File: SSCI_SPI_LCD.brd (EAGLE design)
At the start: 110 x 100 mm, 29 parts, among them IC3 74LVC541_RGY, X1 TSW-108-02-S-S, X2 TSW-108-02-S-S

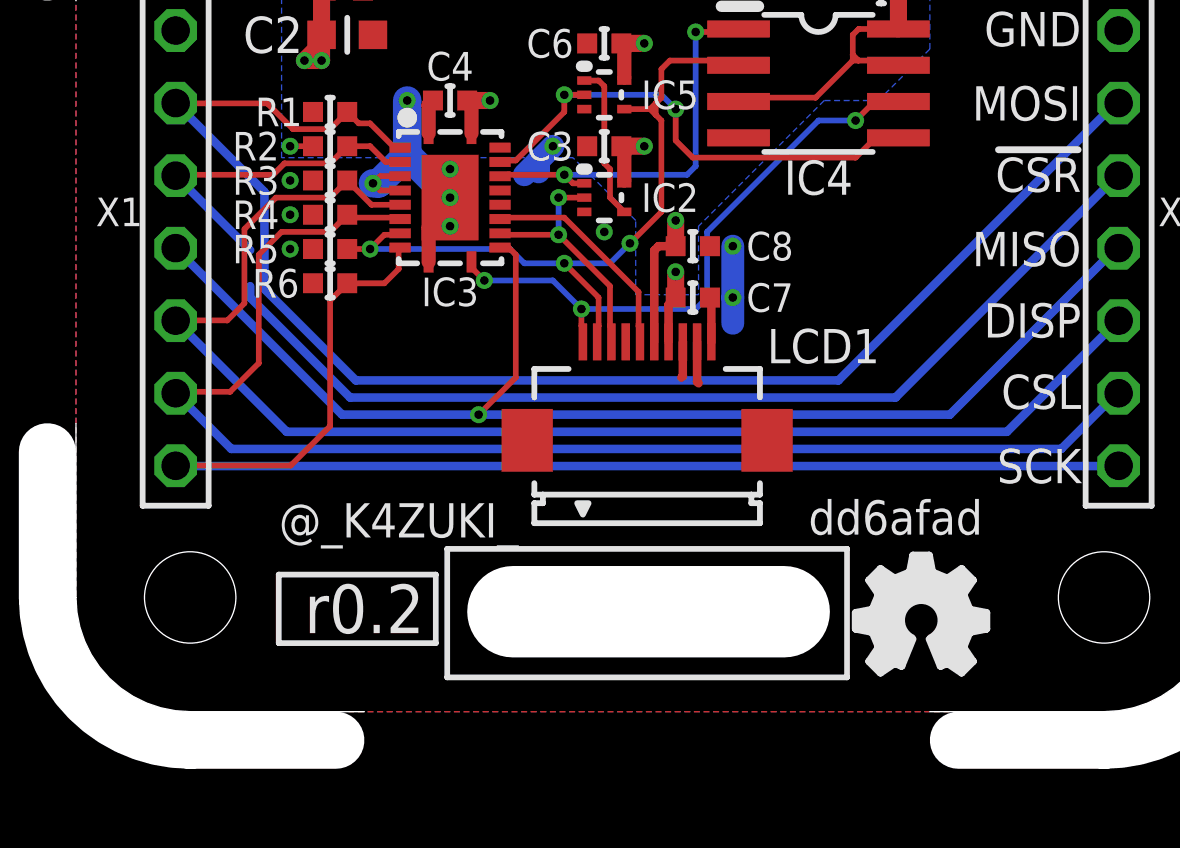
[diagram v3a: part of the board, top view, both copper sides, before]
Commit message: apply changes to panelising file
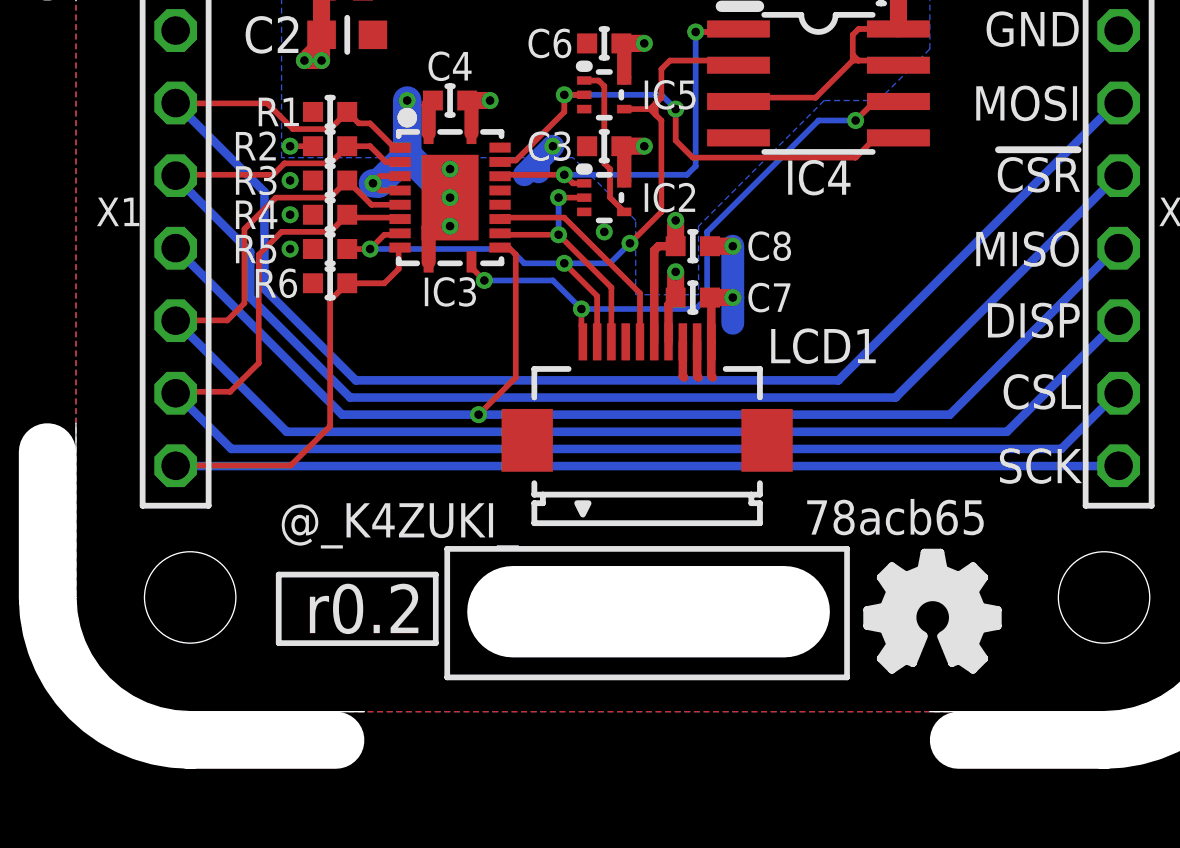
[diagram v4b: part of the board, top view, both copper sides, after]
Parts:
- GIT1: value dd6afad -> 78acb65
- moved ICON2 0.41 mm to (40.0, 13.3)
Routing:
- net GND: track 19.8 -> 22.4 mm
- net !CSR!: track 47.7 -> 48.9 mm
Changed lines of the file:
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@@
 <setting verticaltext="up"/>
 </settings>
-<grid distance="0.1" unitdist="mm" unit="mm" style="dots" multiple="1" display="yes" altdistance="0.1" altunitdist="mm" altunit="mm"/>
+<grid distance="0.1" unitdist="mm" unit="mm" style="dots" multiple="1" display="yes" altdistance="0.05" altunitdist="mm" altunit="mm"/>
 <layers>
 <layer number="1" name="Top" color="12" fill="0" visible="yes" active="yes"/>
@@
 <layer number="45" name="Holes" color="7" fill="1" visible="yes" active="yes"/>
 <layer number="46" name="Milling" color="3" fill="0" visible="yes" active="yes"/>
-<layer number="47" name="Measures" color="7" fill="1" visible="yes" active="yes"/>
+<layer number="47" name="Measures" color="7" fill="1" visible="no" active="yes"/>
 <layer number="48" name="Document" color="7" fill="1" visible="no" active="yes"/>
 <layer number="49" name="Reference" color="7" fill="1" visible="no" active="yes"/>
@@
 <layer number="100" name="Muster" color="7" fill="1" visible="no" active="no"/>
 <layer number="101" name="Attributes" color="7" fill="1" visible="no" active="yes"/>
-<layer number="102" name="Vscore" color="7" fill="1" visible="yes" active="yes"/>
+<layer number="102" name="Vscore" color="7" fill="1" visible="no" active="yes"/>
 <layer number="103" name="tMap" color="7" fill="1" visible="no" active="yes"/>
 <layer number="104" name="Name" color="7" fill="1" visible="no" active="yes"/>
@@
 <wire x1="30.5" y1="25.5" x2="30.5" y2="23.8" width="0" layer="41"/>
 <wire x1="19.8" y1="28.5" x2="20.3" y2="28.5" width="0" layer="41"/>
-<wire x1="21.4" y1="30" x2="21.4" y2="30.5" width="0" layer="41"/>
-<wire x1="20.7" y1="30" x2="20.7" y2="30.5" width="0" layer="41"/>
-<wire x1="20.7" y1="25.5" x2="20.7" y2="26" width="0" layer="41"/>
-<wire x1="21.4" y1="25.5" x2="21.4" y2="26" width="0" layer="41"/>
+<wire x1="22.8" y1="30" x2="22.8" y2="30.5" width="0" layer="41"/>
+<wire x1="21.9" y1="30" x2="21.9" y2="30.5" width="0" layer="41"/>
+<wire x1="21.9" y1="25.5" x2="21.9" y2="26" width="0" layer="41"/>
+<wire x1="22.8" y1="25.6" x2="22.8" y2="26.1" width="0" layer="41"/>
 <wire x1="21.3" y1="25.2" x2="20.8" y2="25.2" width="0" layer="41"/>
-<wire x1="20.8" y1="29.5" x2="22.8" y2="29.5" width="0" layer="41"/>
-<wire x1="22.8" y1="29.5" x2="22.8" y2="26.5" width="0" layer="41"/>
-<wire x1="20.8" y1="26.5" x2="20.8" y2="29.5" width="0" layer="41"/>
+<wire x1="22.1" y1="29.5" x2="24.1" y2="29.5" width="0" layer="41"/>
+<wire x1="24.1" y1="29.5" x2="24.1" y2="26.5" width="0" layer="41"/>
+<wire x1="22.1" y1="26.5" x2="22.1" y2="29.5" width="0" layer="41"/>
 <wire x1="32.6" y1="23.6" x2="32.6" y2="22.3" width="0" layer="41"/>
 <dimension x1="0" y1="0" x2="0" y2="10" x3="-8.6" y3="5" textsize="1.778" layer="47"/>
@@
 <text x="45.2" y="18.6" size="1.2" layer="21" ratio="20" align="center-right">SCK</text>
 <dimension x1="13.49" y1="27.5" x2="46.51" y2="27.5" x3="30" y3="2.9" textsize="1.2" textratio="20" layer="47" dtype="horizontal" unit="inch" visible="yes"/>
+<wire x1="31.9" y1="24.1" x2="32.5" y2="24.1" width="0" layer="41"/>
 </plain>
 <attributes>
@@
 <attribute name="NOT_COMPONENT" value="YES" x="14" y="14" size="1.778" layer="27" rot="R270" display="off"/>
 </element>
-<element name="GIT1" library="git-revision" package="GIT-REVISION_1.2" value="dd6afad" x="38.7" y="16.8">
+<element name="GIT1" library="git-revision" package="GIT-REVISION_1.2" value="78acb65" x="38.7" y="16.8">
 <attribute name="NOT_COMPONENT" value="YES" x="38.7" y="16.8" size="1.778" layer="27" display="off"/>
 </element>
@@
 <attribute name="VALUE" x="31.6" y="26.3" size="1" layer="27" font="vector" align="center"/>
 </element>
-<element name="ICON2" library="mylib" package="ICON_OSHW" value="" x="39.6" y="13.2">
-<attribute name="NOT_COMPONENT" value="YES" x="39.6" y="13.2" size="2" layer="27" ratio="20" display="off"/>
+<element name="ICON2" library="mylib" package="ICON_OSHW" value="" x="40" y="13.3">
+<attribute name="NOT_COMPONENT" value="YES" x="40" y="13.3" size="2" layer="27" ratio="20" display="off"/>
 </element>
 </elements>
@@
 <via x="17.5" y="27.4" extent="1-16" drill="0.3"/>
 <wire x1="31.25" y1="22.95" x2="31.25" y2="21.75" width="0.3" layer="1"/>
-<wire x1="31.25" y1="21.75" x2="31.2" y2="21.7" width="0.3" layer="1"/>
-<wire x1="31.75" y1="22.95" x2="31.75" y2="21.55" width="0.3" layer="1"/>
-<wire x1="31.75" y1="21.55" x2="31.8" y2="21.5" width="0.3" layer="1"/>
+<wire x1="31.25" y1="21.75" x2="31.3" y2="21.7" width="0.3" layer="1"/>
+<wire x1="31.75" y1="22.95" x2="31.75" y2="21.75" width="0.3" layer="1"/>
+<wire x1="31.75" y1="21.75" x2="31.8" y2="21.7" width="0.3" layer="1"/>
 <wire x1="32.25" y1="22.95" x2="32.25" y2="24.45" width="0.3" layer="1"/>
 <wire x1="32.25" y1="24.45" x2="32.2" y2="24.5" width="0.3" layer="1"/>
@@
 <wire x1="26.2" y1="29.3" x2="26.2" y2="28.9" width="0.8" layer="16"/>
 <wire x1="26.2" y1="29.3" x2="25.7" y2="28.8" width="0.8" layer="16"/>
+<wire x1="32.25" y1="22.95" x2="32.25" y2="21.75" width="0.3" layer="1"/>
+<wire x1="32.25" y1="21.75" x2="32.3" y2="21.7" width="0.3" layer="1"/>
+<wire x1="33" y1="24.5" x2="32.2" y2="24.5" width="0.6" layer="1"/>
+<wire x1="33" y1="26.3" x2="32.2" y2="26.3" width="0.6" layer="1"/>
 </signal>
 <signal name="5V">
@@
 <wire x1="13.52" y1="28.8" x2="13.49" y2="28.77" width="0.2" layer="1"/>
 <wire x1="19.6" y1="21" x2="16.1" y2="24.5" width="0.3" layer="16"/>
-<wire x1="16.1" y1="24.5" x2="16.1" y2="24.9" width="0.3" layer="16"/>
-<wire x1="16.1" y1="26.16" x2="13.49" y2="28.77" width="0.3" layer="16"/>
-<wire x1="16.1" y1="24.9" x2="16.1" y2="26.16" width="0" layer="19" extent="16-16"/>
+<wire x1="16.1" y1="24.5" x2="16.1" y2="26.1" width="0.3" layer="16"/>
+<wire x1="13.49" y1="28.77" x2="13.49" y2="28.71" width="0.3" layer="16"/>
+<wire x1="13.49" y1="28.71" x2="16.1" y2="26.1" width="0.3" layer="16"/>
 </signal>
 <signal name="MOSI">
@@
 <via x="20.3" y="26.2" extent="1-16" drill="0.3"/>
 <wire x1="25.2" y1="26.2" x2="25.7" y2="25.7" width="0.2" layer="16"/>
-<wire x1="28.25" y1="22.95" x2="28.25" y2="23.45" width="0.2" layer="1"/>
-<wire x1="28.25" y1="23.45" x2="28.3" y2="23.5" width="0.2" layer="1"/>
-<wire x1="28.3" y1="23.5" x2="28.3" y2="24.5" width="0.2" layer="1"/>
-<wire x1="28.3" y1="24.5" x2="27.1" y2="25.7" width="0.2" layer="1"/>
+<wire x1="28.25" y1="22.95" x2="28.25" y2="24.55" width="0.2" layer="1"/>
+<wire x1="28.25" y1="24.55" x2="27.1" y2="25.7" width="0.2" layer="1"/>
 <via x="27.1" y="25.7" extent="1-16" drill="0.3"/>
 <wire x1="33.2" y1="32.635" x2="32.365" y2="32.635" width="0.2" layer="1"/>
@@
 <contactref element="LCD1" pad="3"/>
 <contactref element="IC3" pad="13"/>
-<wire x1="28.75" y1="22.95" x2="28.75" y2="23.45" width="0.2" layer="1"/>
-<wire x1="28.75" y1="23.45" x2="28.7" y2="23.5" width="0.2" layer="1"/>
+<wire x1="28.75" y1="22.95" x2="28.75" y2="24.85" width="0.2" layer="1"/>
 <wire x1="24.85" y1="26.75" x2="24.9" y2="26.7" width="0.2" layer="1"/>
 <wire x1="24.9" y1="26.7" x2="26.9" y2="26.7" width="0.2" layer="1"/>
@@
 <via x="26.9" y="28" extent="1-16" drill="0.3"/>
 <via x="26.9" y="26.7" extent="1-16" drill="0.3"/>
-<wire x1="28.7" y1="23.5" x2="28.7" y2="24.9" width="0.2" layer="1"/>
-<wire x1="28.7" y1="24.9" x2="26.9" y2="26.7" width="0.2" layer="1"/>
+<wire x1="28.75" y1="24.85" x2="26.9" y2="26.7" width="0.2" layer="1"/>
 </signal>
 <signal name="DISP-">
@@
 <wire x1="24.85" y1="27.25" x2="24.9" y2="27.3" width="0.2" layer="1"/>
 <wire x1="24.9" y1="27.3" x2="27.1" y2="27.3" width="0.2" layer="1"/>
-<wire x1="29.75" y1="22.95" x2="29.75" y2="23.45" width="0.2" layer="1"/>
-<wire x1="29.75" y1="23.45" x2="29.7" y2="23.5" width="0.2" layer="1"/>
-<wire x1="29.7" y1="23.5" x2="29.7" y2="24.7" width="0.2" layer="1"/>
-<wire x1="29.7" y1="24.7" x2="27.1" y2="27.3" width="0.2" layer="1"/>
+<wire x1="29.75" y1="22.95" x2="29.75" y2="24.65" width="0.2" layer="1"/>
+<wire x1="29.75" y1="24.65" x2="27.1" y2="27.3" width="0.2" layer="1"/>
 </signal>
 </signals>

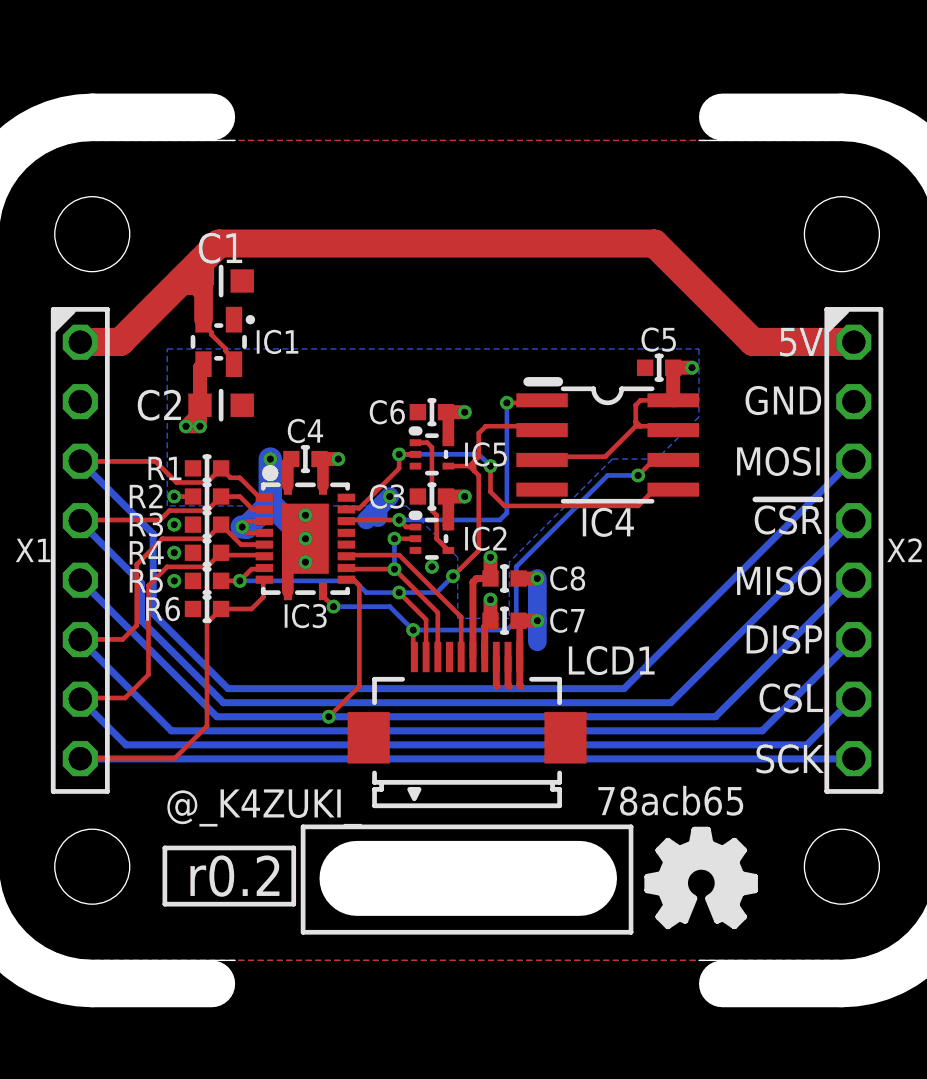
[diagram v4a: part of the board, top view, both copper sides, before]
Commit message: add MinLab icon; moves
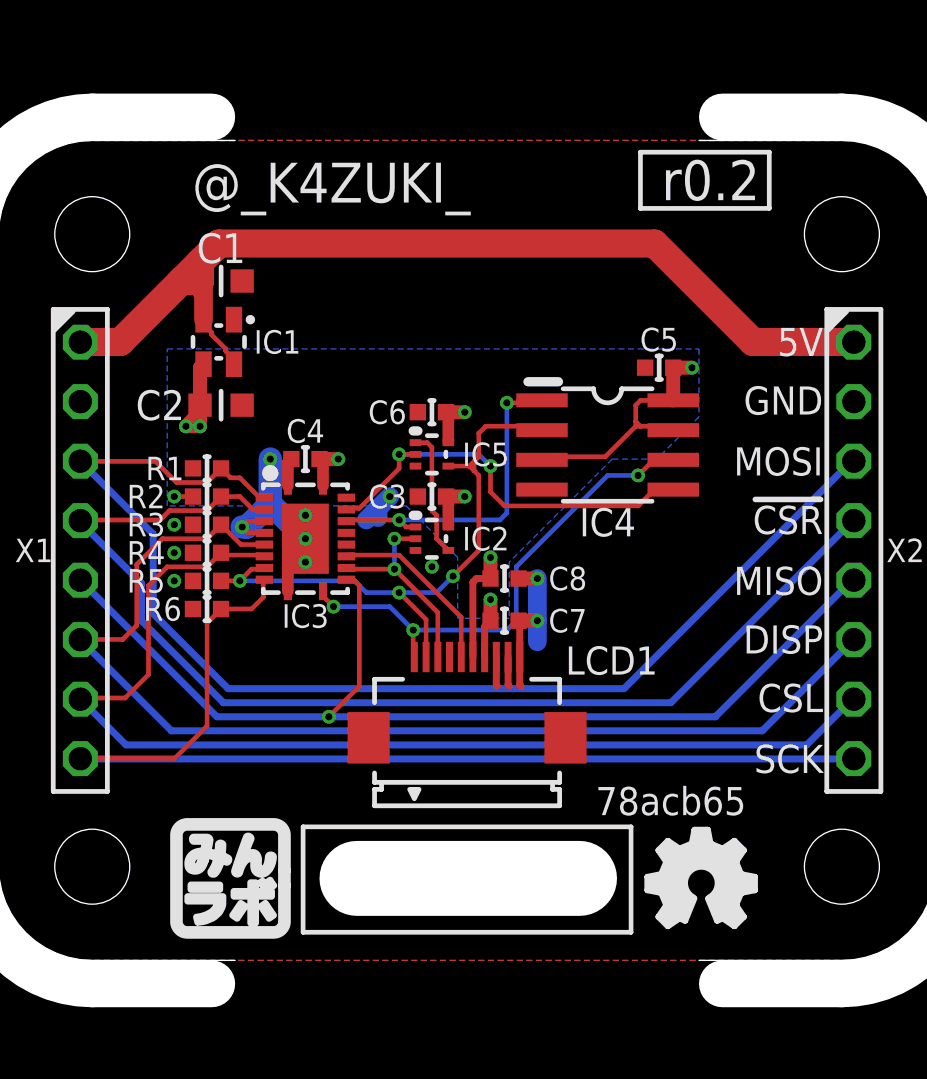
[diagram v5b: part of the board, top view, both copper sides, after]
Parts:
- added I1: (no value), mylib:ICON_MINLAB_5.2MM
- moved ICON1 36.0 mm to (40.5, 43.3)
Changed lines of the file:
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@@
 <dimension x1="0" y1="0" x2="110" y2="0" x3="55" y3="-12.4" textsize="2" textratio="20" layer="47" dtype="horizontal"/>
 <dimension x1="0" y1="0" x2="0" y2="100" x3="-12.6" y3="50" textsize="2" textratio="20" layer="47" dtype="vertical"/>
-<text x="21.3" y="16.7" size="1.2" layer="21" ratio="20" align="center">@_K4ZUKI_</text>
+<text x="24.2" y="43.2" size="1.7" layer="21" ratio="12" align="center">@_K4ZUKI_</text>
 <wire x1="10" y1="45" x2="50" y2="45" width="0.8" layer="41"/>
 <wire x1="10" y1="45" x2="50" y2="45" width="0.8" layer="42"/>
@@
 <attribute name="NOT_COMPONENT" value="YES" x="38.7" y="16.8" size="1.778" layer="27" display="off"/>
 </element>
-<element name="ICON1" library="mylib" package="ICON_REVISION1.7" value="r0.2" x="20.2" y="13.6">
-<attribute name="NOT_COMPONENT" value="YES" x="20.2" y="13.6" size="1.778" layer="27" display="off"/>
+<element name="ICON1" library="mylib" package="ICON_REVISION1.7" value="r0.2" x="40.5" y="43.3">
+<attribute name="NOT_COMPONENT" value="YES" x="40.5" y="43.3" size="1.778" layer="27" display="off"/>
 </element>
 <element name="X1" library="con-samtec.local" package="TSW-108-02-S-S" value="TSW-108-02-S-S" x="13.49" y="27.5" smashed="yes" rot="R90">
@@
 <attribute name="NOT_COMPONENT" value="YES" x="40" y="13.3" size="2" layer="27" ratio="20" display="off"/>
 </element>
+<element name="I1" library="mylib" package="ICON_MINLAB_5.2MM" value="" x="17.4" y="11">
+<attribute name="NOT_COMPONENT" value="YES" x="17.4" y="11" size="1.2" layer="27" ratio="20" display="off"/>
+</element>
 </elements>

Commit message: update libraries; update panelise; update gerbers
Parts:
- GIT1: value 78acb65 -> fd68d81
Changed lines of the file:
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@@
 <attribute name="NAME" x="34.2" y="22.2" size="1.2" layer="25" font="vector" ratio="17"/>
 <attribute name="VALUE" x="25.9" y="22.2" size="1.2" layer="27" font="vector" ratio="17" rot="R180"/>
+<attribute name="MOUSER" value="798-FH12-10S-0.5SH55" x="30" y="19.5" size="1.778" layer="27" display="off"/>
+<attribute name="DIGIKEY" value="HFJ110CT-ND" x="30" y="19.5" size="1.778" layer="27" display="off"/>
 </element>
 <element name="P1" library="mylib" package="PCB_CORNER" value="" x="46" y="14" smashed="yes">
@@
 <attribute name="NOT_COMPONENT" value="YES" x="14" y="14" size="1.778" layer="27" rot="R270" display="off"/>
 </element>
-<element name="GIT1" library="git-revision" package="GIT-REVISION_1.2" value="78acb65" x="38.7" y="16.8">
+<element name="GIT1" library="git-revision" package="GIT-REVISION_1.2" value="fd68d81" x="38.7" y="16.8">
 <attribute name="NOT_COMPONENT" value="YES" x="38.7" y="16.8" size="1.778" layer="27" display="off"/>
 </element>
